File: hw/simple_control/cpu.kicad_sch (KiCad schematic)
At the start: 12 parts, among them J601 Conn_01x04, J602 Raspberry_Pi_0_2_3, J603 Conn_01x03, SW601 SW_Push, U601 PicoW

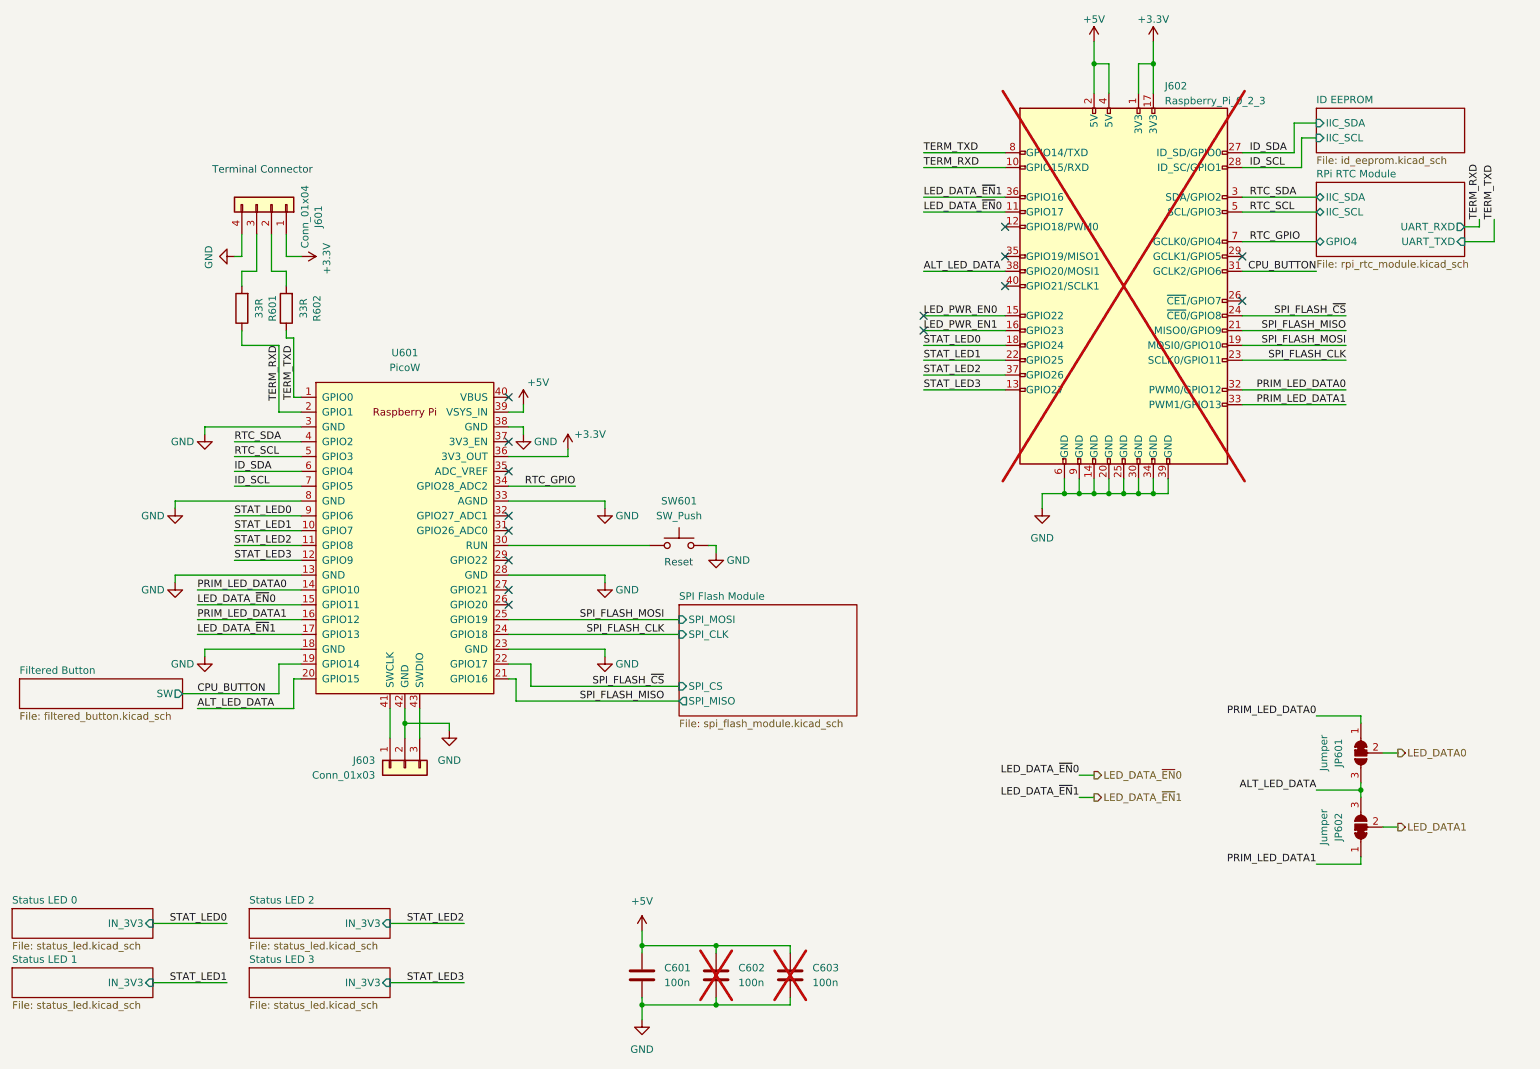
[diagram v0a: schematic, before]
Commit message: chore(hw): add more button connections with interconnections layout
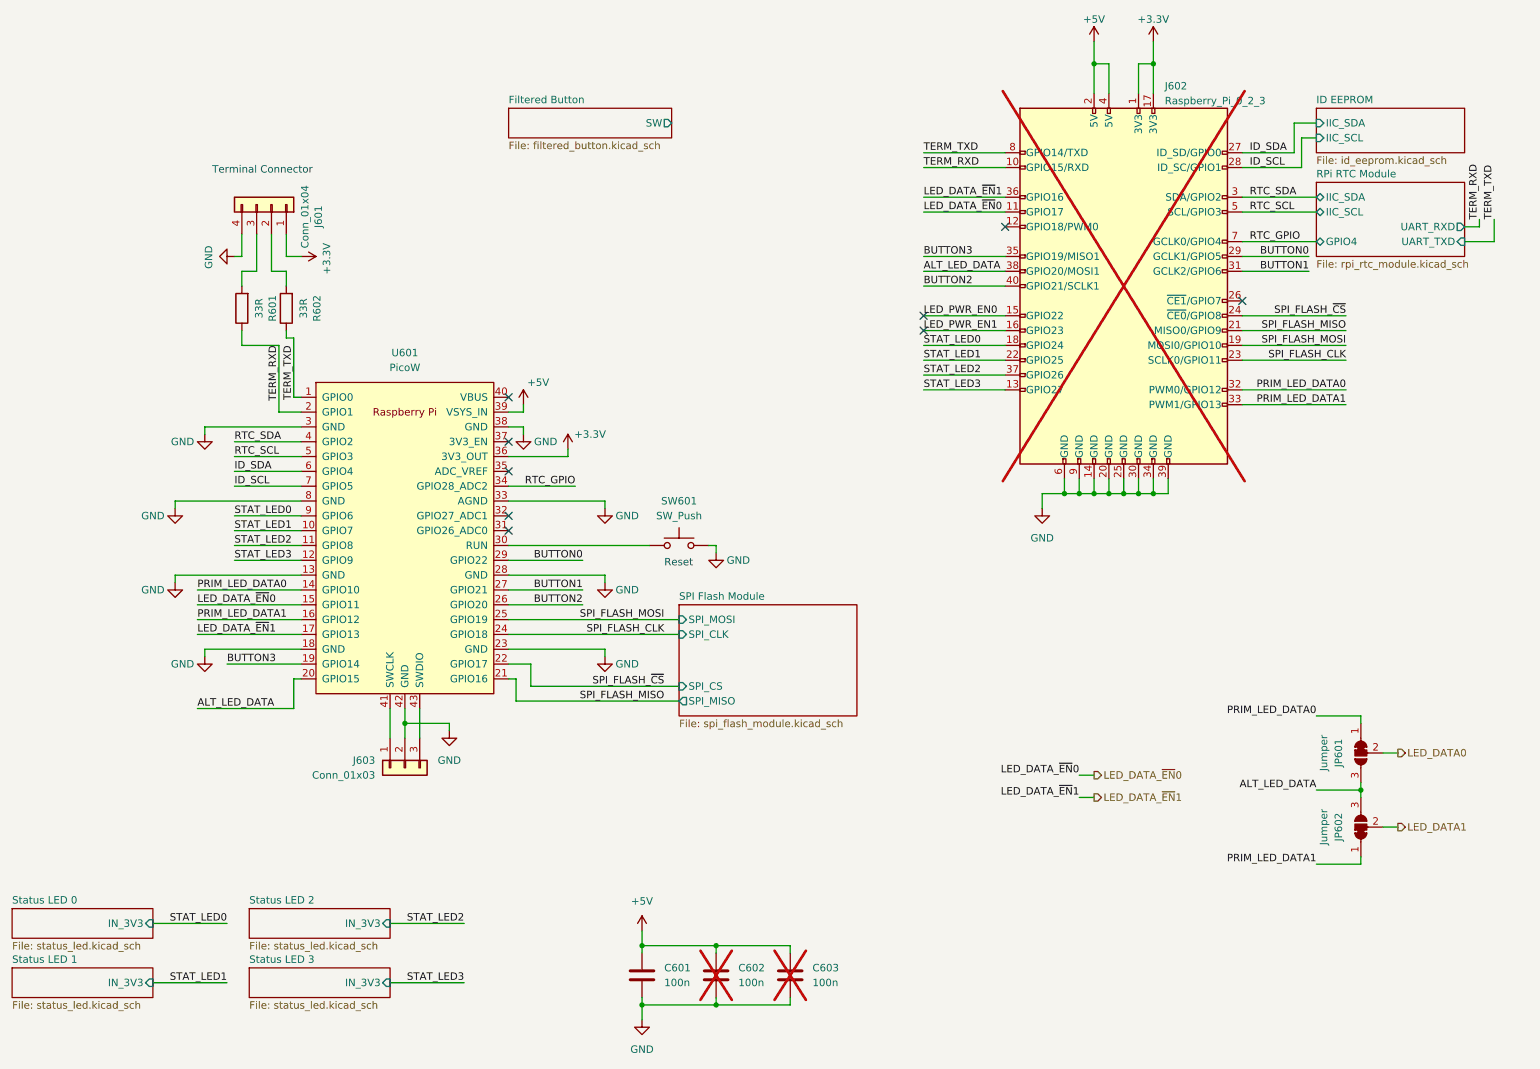
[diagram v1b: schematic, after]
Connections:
- net BUTTON2: now reaches U601.26 (GPIO20)
- net BUTTON2: now also J602.40 (GPIO21/SCLK1)
- net BUTTON1: now reaches U601.27 (GPIO21)
- net BUTTON1: now also J602.31 (GCLK2/GPIO6)
- net BUTTON0: now reaches U601.29 (GPIO22)
- net BUTTON0: now also J602.29 (GCLK1/GPIO5)
- net BUTTON3: now reaches J602.35 (GPIO19/MISO1)
- net BUTTON3: now also U601.19 (GPIO14)
- removed net CPU_BUTTON: J602.31 (GCLK2/GPIO6), U601.19 (GPIO14)
- no-connect marks 15 -> 9
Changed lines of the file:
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@@
   (junction (at 210.82 97.79) (diameter 0) (color 0 0 0 0)
   )
-  (no_connect (at 238.76 64.77))
-  (no_connect (at 238.76 57.15))
-  (no_connect (at 113.03 114.3))
-  (no_connect (at 198.12 62.23))
+  (no_connect (at 198.12 52.07))
   (no_connect (at 113.03 104.14))
-  (no_connect (at 198.12 57.15))
-  (no_connect (at 113.03 109.22))
   (no_connect (at 113.03 93.98))
   (no_connect (at 113.03 88.9))
-  (no_connect (at 198.12 52.07))
+  (no_connect (at 238.76 64.77))
   (no_connect (at 113.03 101.6))
-  (no_connect (at 113.03 116.84))
   (no_connect (at 113.03 81.28))
   (no_connect (at 184.15 69.85))
@@
     (stroke (width 0) (type default))
   )
+  (wire (pts (xy 198.12 62.23) (xy 184.15 62.23))
+    (stroke (width 0) (type default))
+  )
   (wire (pts (xy 52.07 171.45) (xy 64.77 171.45))
     (stroke (width 0) (type default))
@@
     (stroke (width 0) (type default))
   )
+  (wire (pts (xy 238.76 59.69) (xy 250.19 59.69))
+    (stroke (width 0) (type default))
+  )
+  (wire (pts (xy 113.03 109.22) (xy 125.73 109.22))
+    (stroke (width 0) (type default))
+  )
   (wire (pts (xy 60.96 124.46) (xy 77.47 124.46))
     (stroke (width 0) (type default))
@@
     (stroke (width 0) (type default))
   )
+  (wire (pts (xy 113.03 114.3) (xy 125.73 114.3))
+    (stroke (width 0) (type default))
+  )
   (wire (pts (xy 115.57 83.82) (xy 115.57 82.55))
     (stroke (width 0) (type default))
@@
     (stroke (width 0) (type default))
   )
-  (wire (pts (xy 238.76 59.69) (xy 251.46 59.69))
+  (wire (pts (xy 238.76 57.15) (xy 250.19 57.15))
     (stroke (width 0) (type default))
   )
@@
     (stroke (width 0) (type default))
   )
+  (wire (pts (xy 77.47 127) (xy 64.77 127))
+    (stroke (width 0) (type default))
+  )
   (wire (pts (xy 59.69 121.92) (xy 77.47 121.92))
     (stroke (width 0) (type default))
@@
     (stroke (width 0) (type default))
   )
-  (wire (pts (xy 73.66 132.08) (xy 57.15 132.08))
-    (stroke (width 0) (type default))
-  )
   (wire (pts (xy 67.31 53.34) (xy 67.31 57.15))
     (stroke (width 0) (type default))
@@
     (stroke (width 0) (type default))
   )
+  (wire (pts (xy 113.03 116.84) (xy 125.73 116.84))
+    (stroke (width 0) (type default))
+  )
   (wire (pts (xy 76.2 129.54) (xy 77.47 129.54))
     (stroke (width 0) (type default))
@@
     (stroke (width 0) (type default))
   )
-  (wire (pts (xy 73.66 127) (xy 77.47 127))
-    (stroke (width 0) (type default))
-  )
   (wire (pts (xy 210.82 95.25) (xy 210.82 97.79))
     (stroke (width 0) (type default))
@@
     (stroke (width 0) (type default))
   )
-  (wire (pts (xy 73.66 132.08) (xy 73.66 127))
+  (wire (pts (xy 198.12 57.15) (xy 184.15 57.15))
     (stroke (width 0) (type default))
   )
@@
     (effects (font (size 1.27 1.27)) (justify right bottom))
   )
+  (label "BUTTON2" (at 184.15 62.23 0) (fields_autoplaced)
+    (effects (font (size 1.27 1.27)) (justify left bottom))
+  )
   (label "STAT_LED1" (at 64.77 181.61 180) (fields_autoplaced)
     (effects (font (size 1.27 1.27)) (justify right bottom))
@@
     (effects (font (size 1.27 1.27)) (justify left bottom))
   )
+  (label "BUTTON1" (at 250.19 59.69 180) (fields_autoplaced)
+    (effects (font (size 1.27 1.27)) (justify right bottom))
+  )
   (label "SPI_FLASH_MISO" (at 256.54 69.85 180) (fields_autoplaced)
     (effects (font (size 1.27 1.27)) (justify right bottom))
@@
     (effects (font (size 1.27 1.27)) (justify left bottom))
   )
-  (label "CPU_BUTTON" (at 59.69 132.08 0) (fields_autoplaced)
+  (label "BUTTON3" (at 184.15 57.15 0) (fields_autoplaced)
     (effects (font (size 1.27 1.27)) (justify left bottom))
   )
@@
     (effects (font (size 1.27 1.27)) (justify right bottom))
   )
+  (label "BUTTON3" (at 64.77 127 0) (fields_autoplaced)
+    (effects (font (size 1.27 1.27)) (justify left bottom))
+  )
+  (label "BUTTON1" (at 125.73 114.3 180) (fields_autoplaced)
+    (effects (font (size 1.27 1.27)) (justify right bottom))
+  )
   (label "TERM_RXD" (at 279.4 50.8 90) (fields_autoplaced)
     (effects (font (size 1.27 1.27)) (justify left bottom))
@@
     (effects (font (size 1.27 1.27)) (justify left bottom))
   )
-  (label "CPU_BUTTON" (at 251.46 59.69 180) (fields_autoplaced)
+  (label "BUTTON0" (at 250.19 57.15 180) (fields_autoplaced)
     (effects (font (size 1.27 1.27)) (justify right bottom))
   )
@@
     (effects (font (size 1.27 1.27)) (justify left bottom))
   )
+  (label "BUTTON0" (at 125.73 109.22 180) (fields_autoplaced)
+    (effects (font (size 1.27 1.27)) (justify right bottom))
+  )
   (label "STAT_LED2" (at 184.15 77.47 0) (fields_autoplaced)
     (effects (font (size 1.27 1.27)) (justify left bottom))
@@
   (label "TERM_RXD" (at 184.15 41.91 0) (fields_autoplaced)
     (effects (font (size 1.27 1.27)) (justify left bottom))
+  )
+  (label "BUTTON2" (at 125.73 116.84 180) (fields_autoplaced)
+    (effects (font (size 1.27 1.27)) (justify right bottom))
   )
   (label "ALT_LED_DATA" (at 251.46 148.59 180) (fields_autoplaced)
@@
     )
   )
-  (sheet (at 29.21 129.54) (size 27.94 5.08) (fields_autoplaced)
+  (sheet (at 113.03 31.75) (size 27.94 5.08) (fields_autoplaced)
     (stroke (width 0.1524) (type solid))
     (fill (color 0 0 0 0.0000))
-    (property "Sheetname" "Filtered Button" (at 29.21 128.8284 0)
+    (property "Sheetname" "Filtered Button" (at 113.03 31.0384 0)
       (effects (font (size 1.27 1.27)) (justify left bottom))
     )
-    (property "Sheetfile" "filtered_button.kicad_sch" (at 29.21 135.2046 0)
+    (property "Sheetfile" "filtered_button.kicad_sch" (at 113.03 37.4146 0)
       (effects (font (size 1.27 1.27)) (justify left top))
     )
-    (pin "SW" output (at 57.15 132.08 0)
+    (pin "SW" output (at 140.97 34.29 0)
       (effects (font (size 1.27 1.27)) (justify right))
     )
